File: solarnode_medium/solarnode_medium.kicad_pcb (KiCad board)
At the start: 2 copper layers, 97 parts, among them J1 Conn_01x06, Q1 AO3400, Q2 AO3400, Q3 AO3400, Q4 AO3400, SW1 3*4*2mm, U1 YX59012, U2 SGM2033-3.3, U3 MAX485E, U4 SGM48211, U5 SGM48211, U6 LM358, U7 YX59012

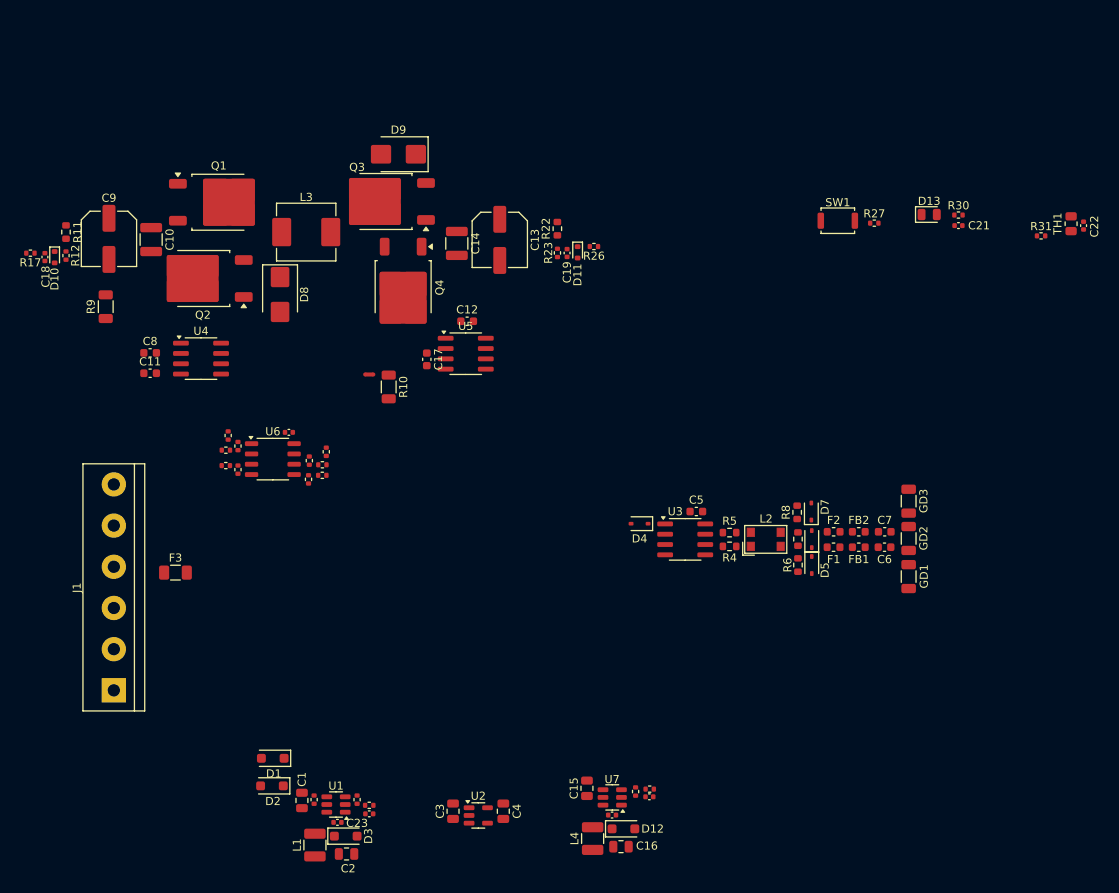
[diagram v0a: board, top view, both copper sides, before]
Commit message: 微调原理图，PCB布局调整，划定边框
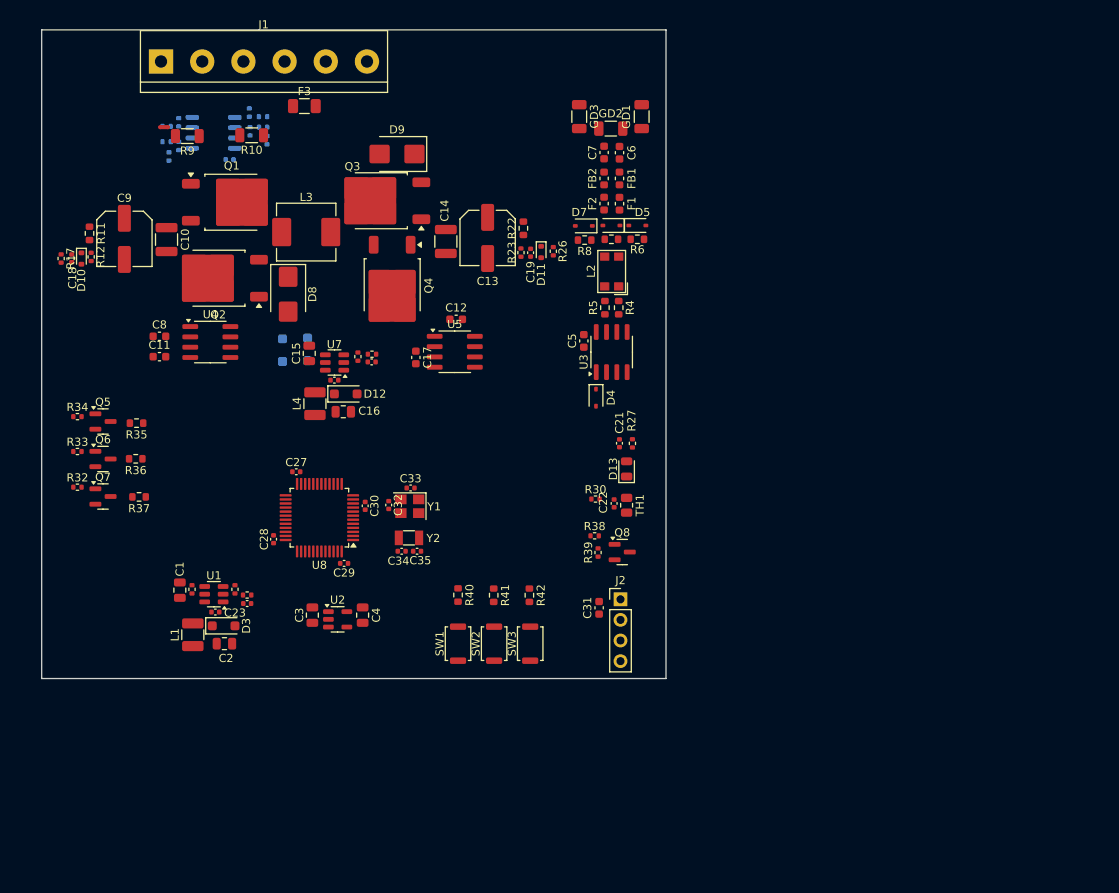
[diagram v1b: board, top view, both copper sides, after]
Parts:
- removed R31: 10k, Resistor_SMD:R_0402_1005Metric
- added C27: 0.1uf, Capacitor_SMD:C_0402_1005Metric, F.Cu at (101.1, 99.3)
- added C28: 0.1uf, Capacitor_SMD:C_0402_1005Metric, F.Cu at (98.3, 107.6)
- added C29: 0.1uf, Capacitor_SMD:C_0402_1005Metric, F.Cu at (107.0, 110.6)
- added C30: 0.1uf, Capacitor_SMD:C_0402_1005Metric, F.Cu at (109.6, 103.5)
- added C31: 0.1uf, Capacitor_SMD:C_0603_1608Metric, F.Cu at (138.4, 116.1)
- added C32: C_Small, Capacitor_SMD:C_0402_1005Metric, F.Cu at (112.5, 103.4)
- added C33: C_Small, Capacitor_SMD:C_0402_1005Metric, F.Cu at (115.2, 101.3)
- added C34: C_Small, Capacitor_SMD:C_0402_1005Metric, F.Cu at (114.1, 109.1)
- added C35: C_Small, Capacitor_SMD:C_0402_1005Metric, F.Cu at (116.0, 109.1)
- added J2: Conn_01x04, Connector_PinHeader_2.54mm:PinHeader_1x04_P2.54mm_Vertical, F.Cu at (141.1, 115.0)
- added Q5: Q_NPN_BEC, Package_TO_SOT_SMD:SOT-23, F.Cu at (77.3, 93.1)
- added Q6: Q_NPN_BEC, Package_TO_SOT_SMD:SOT-23, F.Cu at (77.3, 97.7)
- added Q7: Q_NPN_BEC, Package_TO_SOT_SMD:SOT-23, F.Cu at (77.3, 102.3)
- added Q8: Q_NMOS_GSD, Package_TO_SOT_SMD:SOT-23, F.Cu at (141.3, 109.2)
- added R32: 4.7k, Resistor_SMD:R_0402_1005Metric, F.Cu at (74.1, 101.2)
- added R33: 4.7k, Resistor_SMD:R_0402_1005Metric, F.Cu at (74.1, 96.8)
- added R34: 4.7k, Resistor_SMD:R_0402_1005Metric, F.Cu at (74.1, 92.5)
- added R35: 150, Resistor_SMD:R_0603_1608Metric, F.Cu at (81.4, 93.3)
- added R36: 150, Resistor_SMD:R_0603_1608Metric, F.Cu at (81.3, 97.7)
- added R37: 150, Resistor_SMD:R_0603_1608Metric, F.Cu at (81.7, 102.4)
- added R38: 1k, Resistor_SMD:R_0402_1005Metric, F.Cu at (137.9, 107.2)
- added R39: 100k, Resistor_SMD:R_0402_1005Metric, F.Cu at (138.3, 109.3)
- added R40: R, Resistor_SMD:R_0603_1608Metric, F.Cu at (121.0, 114.5)
- added R41: R, Resistor_SMD:R_0603_1608Metric, F.Cu at (125.5, 114.5)
- added R42: R, Resistor_SMD:R_0603_1608Metric, F.Cu at (129.8, 114.5)
- added SW2: SW_Push, Button_Switch_SMD:SW_Push_SPST_NO_Alps_SKRK, F.Cu at (125.5, 120.5)
- added SW3: SW_Push, Button_Switch_SMD:SW_Push_SPST_NO_Alps_SKRK, F.Cu at (129.9, 120.5)
- added U8: CH32V203C8T6, Package_QFP:LQFP-48_7x7mm_P0.5mm, F.Cu at (104.0, 105.0)
- added Y1: Crystal_GND24_Small, Crystal:Crystal_SMD_3225-4Pin_3.2x2.5mm, F.Cu at (115.1, 103.5)
- added Y2: Crystal_Small, Crystal:Crystal_SMD_3215-2Pin_3.2x1.5mm, F.Cu at (115.0, 107.5)
- C20, D1, D2, R13, R14, R15, R16, R18, R19, R20, R21, R24, R25, U6: moved to B.Cu
- SW1: value 3*4*2mm -> SW_Push
- moved J1 77.8 mm to (84.4, 48.7), turned to 0 degrees
- moved SW1 70.1 mm to (121.0, 120.5), turned to 90 degrees
- moved C22 67.3 mm to (140.3, 103.2), turned to -90 degrees
- moved GD1 65.6 mm to (143.7, 55.5), turned to 90 degrees
- moved TH1 64.9 mm to (141.8, 103.4), turned to -90 degrees
- moved R28 63.6 mm to (108.7, 85.1)
- moved C15 63.6 mm to (102.7, 84.7)
- moved D12 63.6 mm to (107.2, 89.7)
- moved R29 63.6 mm to (110.4, 84.8)
- moved U7 63.6 mm to (105.8, 85.8)
- moved C25 63.6 mm to (105.8, 88.0)
- moved C16 63.6 mm to (106.9, 91.9)
- moved C26 63.6 mm to (110.4, 85.8)
- moved L4 63.6 mm to (103.4, 90.9)
- moved GD2 62.5 mm to (139.9, 57.0), turned to 180 degrees
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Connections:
- net /Power/485+ renamed /485+
- net /Power/485- renamed /485-
- net /Power/DC12V_EN renamed /MCU and Commication/DC12V_EN
- C10 pad 1: /DC-DC/SLR+ -> /SLR+
- C13 pad 1: /DC-DC/BUS+ -> /BUS+
- C14 pad 1: /DC-DC/BUS+ -> /BUS+
- C21 pad 1: /ADC_PD -> /MCU and Commication/ADC_PD
- C22 pad 1: /ADC_T -> /MCU and Commication/ADC_T
- C9 pad 1: /DC-DC/SLR+ -> /SLR+
- D1 pad 2: /Power/SLR+ -> /SLR+
- D13 pad 1: /SampEn -> /MCU and Commication/SampEn
- D13 pad 2: /ADC_PD -> /MCU and Commication/ADC_PD
- D2 pad 2: /Power/BUS+ -> /BUS+
- D9 pad 1: /DC-DC/BUS+ -> /BUS+
- F3 pad 2: /Power/BUS+ -> /BUS+
- J1 pad 1: /Power/SLR+ -> /SLR+
- J1 pad 2: /Power/SLR- -> /SLR-
- J1 pad 3: /Power/BUS- -> /BUS-
- Q1 pad 3: /DC-DC/SLR+ -> /SLR+
- Q3 pad 3: /DC-DC/BUS+ -> /BUS+
- R10 pad 2: /DC-DC/BUS- -> /BUS-
- R11 pad 1: /DC-DC/SLR+ -> /SLR+
- R14 pad 1: /DC-DC/SLR- -> /SLR-
- R15 pad 1: /DC-DC/BUS- -> /BUS-
- R22 pad 1: /DC-DC/BUS+ -> /BUS+
- R27 pad 1: /PUSH -> /MCU and Commication/ADC_PD
- R30 pad 1: /ADC_PD -> /MCU and Commication/SampEn
- R30 pad 2: GND -> /MCU and Commication/ADC_T
- R9 pad 1: /DC-DC/SLR- -> /SLR-
- SW1 pad 1: +3.3V -> GND
- SW1 pad 2: /PUSH -> /MCU and Commication/KEY1
- TH1 pad 1: /ADC_T -> /MCU and Commication/ADC_T
- U4 pad 5: unconnected-(U4-HI-Pad5) -> /DC-DC/Driver_1H
- U4 pad 6: unconnected-(U4-LI-Pad6) -> /DC-DC/Driver_1L
- U5 pad 5: unconnected-(U5-HI-Pad5) -> /DC-DC/Driver_2H
- U5 pad 6: unconnected-(U5-LI-Pad6) -> /DC-DC/Driver_2L
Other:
- board outline added: 77 x 80 mm

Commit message: 微调原理图，连接局部走线
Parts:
- moved C8 6.85 mm to (90.5, 79.8)
- moved C11 2.08 mm to (86.0, 84.1), turned to -90 degrees
- moved C18 1.46 mm to (74.8, 72.8)
- moved D10 0.96 mm to (73.7, 72.9)
- moved C5 0.94 mm to (136.6, 82.2)
- moved D4 0.94 mm to (138.1, 89.2)
- moved U3 0.94 mm to (140.0, 83.6)
- moved R4 0.73 mm to (140.9, 78.3)
- moved R5 0.73 mm to (139.2, 78.3)
- moved L2 0.60 mm to (140.0, 74.0)
- moved C12 0.55 mm to (120.8, 81.0)
- moved GD1 0.54 mm to (143.8, 56.0)
- moved GD2 0.54 mm to (140.0, 57.5)
- moved GD3 0.54 mm to (136.1, 56.0)
- moved C26 0.45 mm to (110.0, 85.7)
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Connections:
- Q5 pad 2: Net-(Q5-E) -> GND
- Q6 pad 2: Net-(Q5-E) -> GND
- Q7 pad 2: Net-(Q5-E) -> GND
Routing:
- net GND: track 0.00 -> 260.5 mm
- net /BUS+: track 0.00 -> 35.9 mm
- net /SLR+: track 0.00 -> 35.0 mm
- net +3.3V: track 0.00 -> 31.8 mm
- net /DC-DC/Driver_2H: track 0.00 -> 30.9 mm, vias 0 -> 2
- net /DC-DC/Driver_2L: track 0.00 -> 30.8 mm, vias 0 -> 2
- net /DC-DC/Driver_1H: track 0.00 -> 23.2 mm
- net /DC-DC/Driver_1L: track 0.00 -> 22.6 mm
- net /DC-DC/MOS1_G: track 0.00 -> 20.1 mm, vias 0 -> 2
- net +12V: track 0.00 -> 19.5 mm
- net +5V: track 0.00 -> 19.0 mm
- net /DC-DC/MOS4_G: track 0.00 -> 18.4 mm, vias 0 -> 2
- net Net-(D9-A): track 0.00 -> 18.3 mm
- net Net-(D8-K): track 0.00 -> 15.5 mm
- net /DC-DC/MOS3_G: track 0.00 -> 15.3 mm, vias 0 -> 2
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
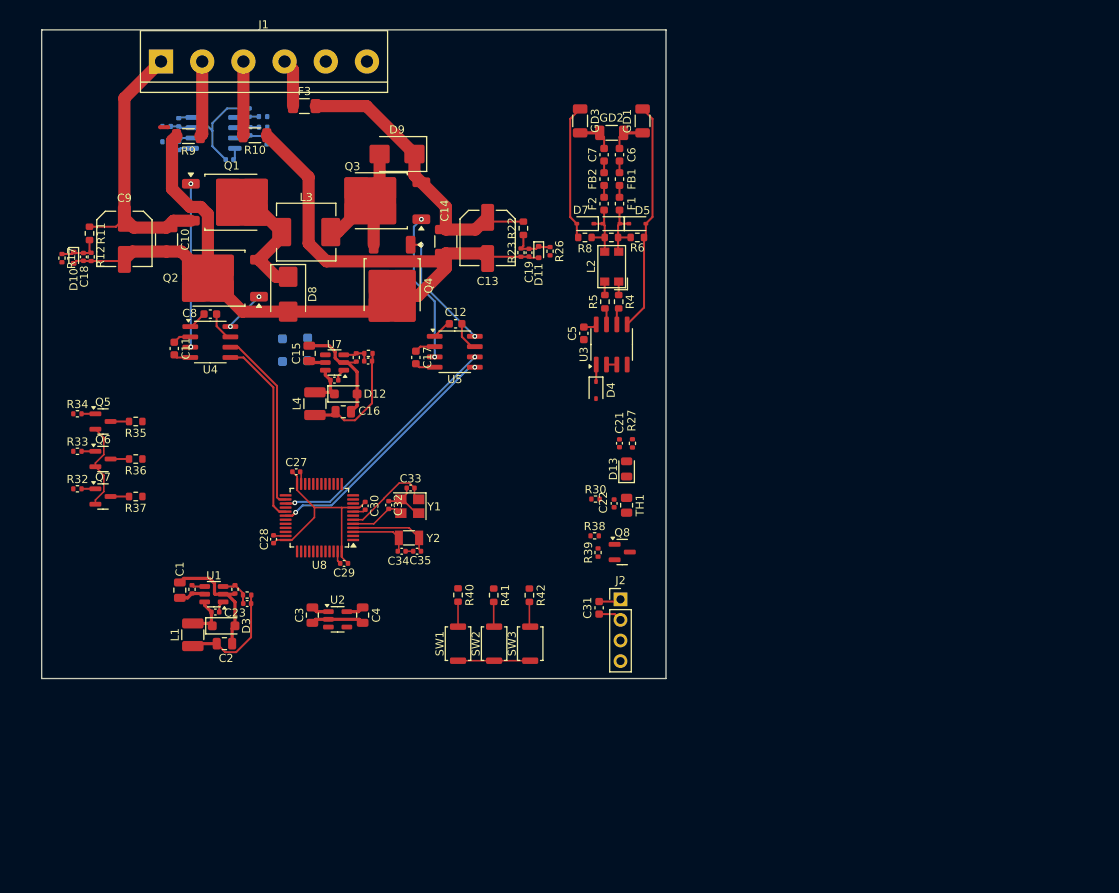
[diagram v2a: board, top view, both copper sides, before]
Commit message: 原理图分配一些MCU引脚，PCB连接走线，添加覆铜
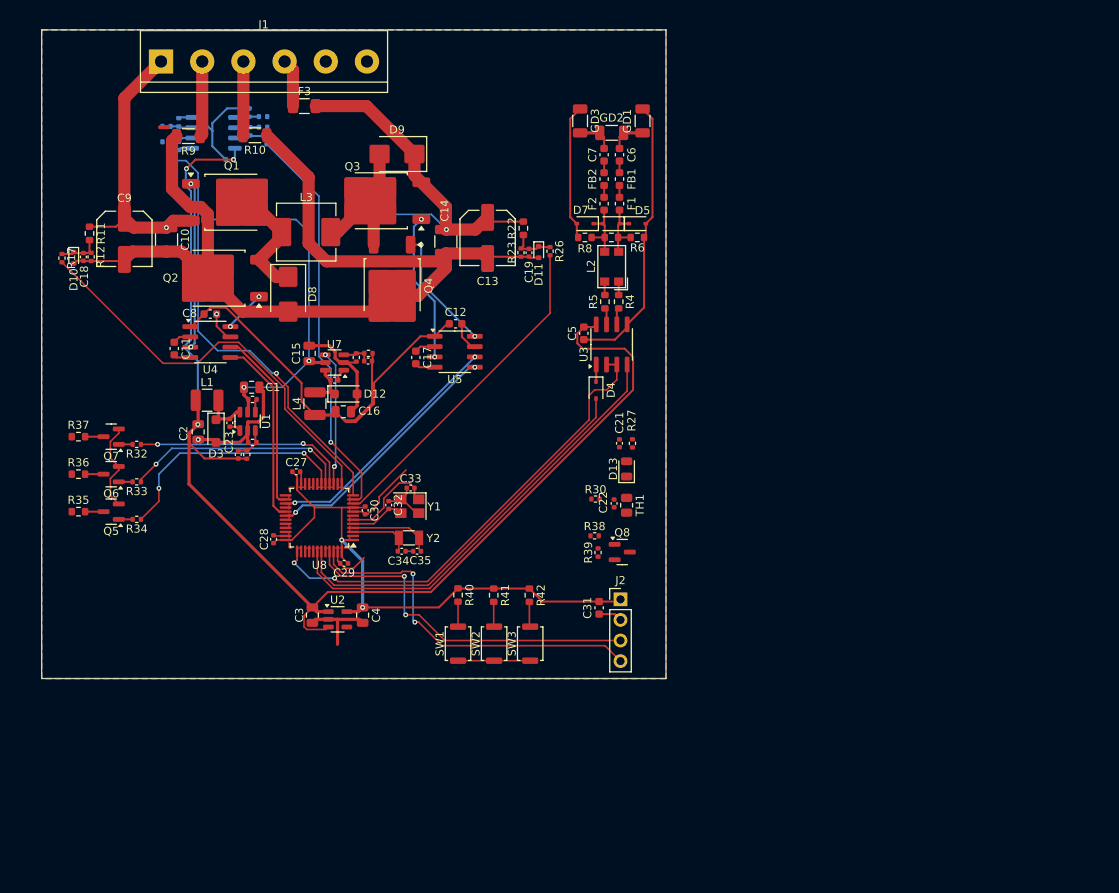
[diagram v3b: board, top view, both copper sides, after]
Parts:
- moved L1 29.0 mm to (90.1, 90.5), turned to 180 degrees
- moved C1 26.5 mm to (95.6, 88.9), turned to 180 degrees
- moved C2 26.3 mm to (89.0, 94.4), turned to -90 degrees
- moved R1 24.6 mm to (95.7, 90.4), turned to 0 degrees
- moved D3 24.0 mm to (91.2, 94.3), turned to -90 degrees
- moved C23 23.4 mm to (92.9, 93.3), turned to 90 degrees
- moved U1 21.7 mm to (95.1, 93.1), turned to 90 degrees
- moved D1 19.4 mm to (88.5, 68.2), turned to 180 degrees
- moved C24 18.4 mm to (93.9, 97.2), turned to -90 degrees
- moved R2 18.2 mm to (95.7, 95.7), turned to 0 degrees
- moved R3 17.3 mm to (95.0, 97.2), turned to -90 degrees
- moved R34 14.9 mm to (81.4, 105.2), turned to 180 degrees
- moved D2 14.5 mm to (104.1, 69.8), turned to 0 degrees
- moved R35 13.2 mm to (74.2, 104.2), turned to 0 degrees
- moved Q5 11.2 mm to (78.3, 104.2), turned to 180 degrees
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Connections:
- U8 pad 10: unconnected-(U8-PA0-Pad10) -> /DC-DC/ADC_Vbus
- U8 pad 11: unconnected-(U8-PA1-Pad11) -> /DC-DC/ADC_Ibus
- U8 pad 12: unconnected-(U8-PA2-Pad12) -> /DC-DC/ADC_Islr
- U8 pad 13: unconnected-(U8-PA3-Pad13) -> /DC-DC/ADC_Vslr
- U8 pad 15: unconnected-(U8-PA5-Pad15) -> /MCU and Commication/DC12V_EN
- U8 pad 37: unconnected-(U8-PA14-Pad37) -> /MCU and Commication/MAX485_TR
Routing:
- net +5V: track 19.0 -> 158.1 mm, vias 0 -> 3
- net /MCU and Commication/MAX485_TR: track 1.27 -> 57.5 mm, vias 0 -> 2
- net /MCU and Commication/MAX485_DI: track 0.00 -> 55.0 mm
- net /DC-DC/ADC_Islr: track 0.00 -> 54.5 mm, vias 0 -> 1
- net /DC-DC/ADC_Vslr: track 0.00 -> 50.8 mm
- net /DC-DC/ADC_Ibus: track 0.00 -> 49.6 mm, vias 0 -> 1
- net /MCU and Commication/MAX485_RO: track 0.00 -> 48.0 mm
- net /MCU and Commication/SDA: track 0.00 -> 45.4 mm, vias 0 -> 2
- net /MCU and Commication/SCL: track 0.00 -> 44.1 mm, vias 0 -> 2
- net +3.3V: track 31.8 -> 73.2 mm, vias 0 -> 2
- net /DC-DC/ADC_Vbus: track 0.00 -> 41.2 mm
- net VINP: track 5.38 -> 44.0 mm, vias 0 -> 2
- net +12V: track 19.5 -> 57.5 mm
- net /MCU and Commication/LED_B: track 0.00 -> 30.1 mm, vias 0 -> 2
- net /MCU and Commication/LED_G: track 0.00 -> 27.9 mm, vias 0 -> 2
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- added copper zone on F.Cu, net +3.3V
- added copper zone on B.Cu, net GND
- added copper zone on F.Cu, net GND

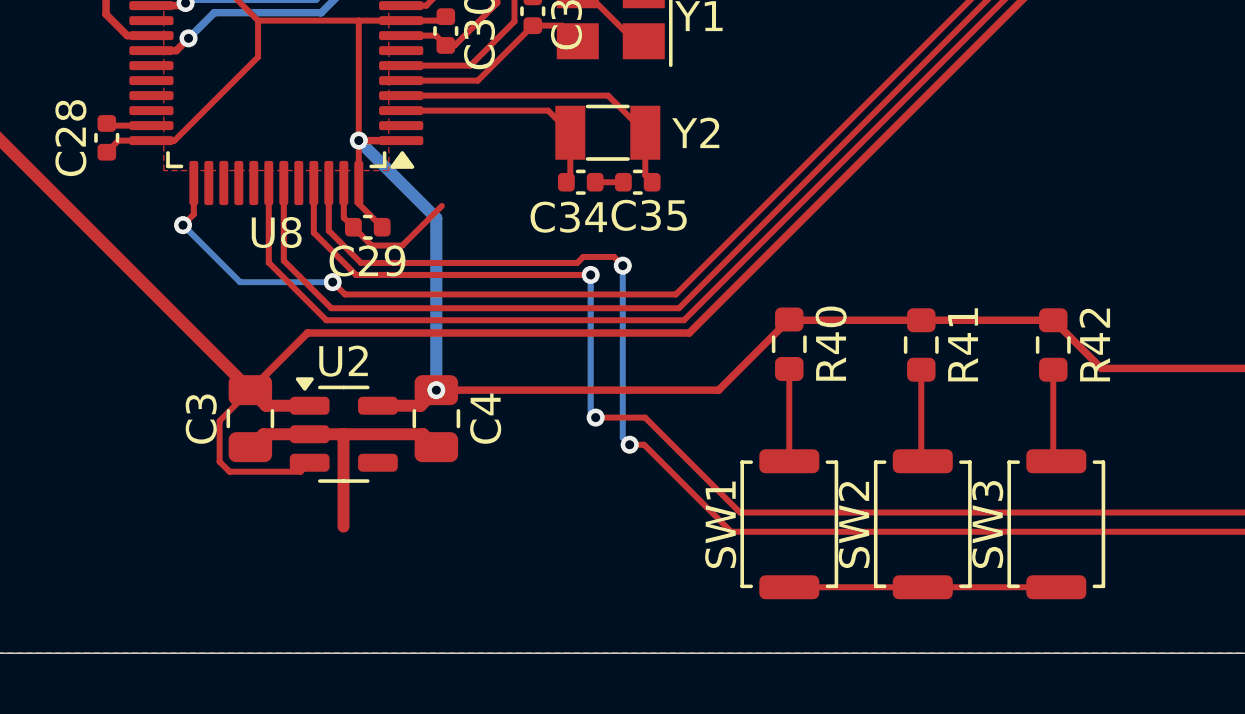
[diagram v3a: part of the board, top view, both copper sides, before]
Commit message: 连接按键，取消SPI接口
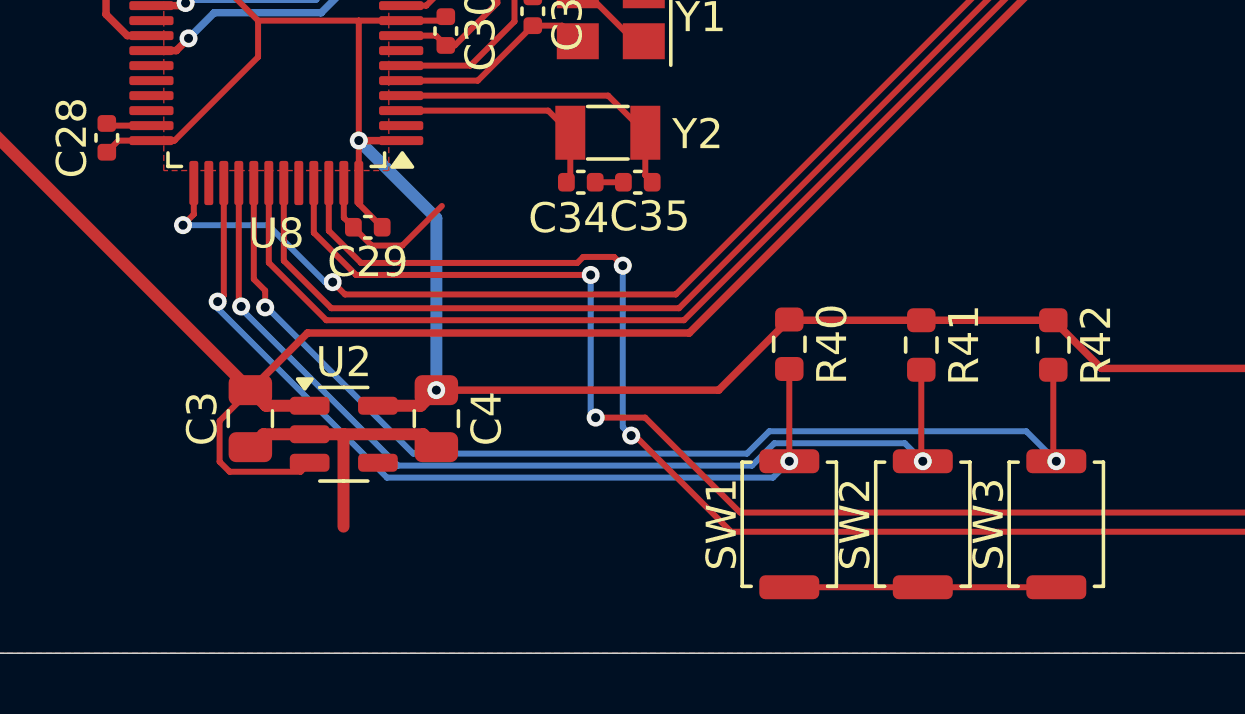
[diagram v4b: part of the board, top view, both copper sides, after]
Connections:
- U8 pad 39: /MCU and Commication/SCK -> /MCU and Commication/KEY1
- U8 pad 40: /MCU and Commication/MISO -> /MCU and Commication/KEY2
- U8 pad 41: /MCU and Commication/MOSI -> /MCU and Commication/KEY3
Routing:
- net /MCU and Commication/KEY3: track 3.09 -> 36.5 mm, vias 0 -> 2
- net /MCU and Commication/KEY2: track 3.07 -> 32.7 mm, vias 0 -> 2
- net /MCU and Commication/KEY1: track 3.08 -> 29.0 mm, vias 0 -> 2

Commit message: 连接蜂鸣器驱动电路
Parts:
- moved Q8 63.2 mm to (78.1, 111.2), turned to 180 degrees
- moved R39 57.3 mm to (81.1, 111.1), turned to 90 degrees
- moved R38 56.7 mm to (81.5, 113.2), turned to 180 degrees
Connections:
- U8 pad 19: unconnected-(U8-PB1-Pad19) -> /MCU and Commication/SPK
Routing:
- net /MCU and Commication/SPK: track 0.00 -> 36.8 mm, vias 0 -> 2
- net Net-(Q8-G): track 0.00 -> 3.84 mm
- net GND: track 281.5 -> 283.7 mm
